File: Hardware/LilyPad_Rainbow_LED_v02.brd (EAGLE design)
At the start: 38.6 x 12.7 mm, 37 parts

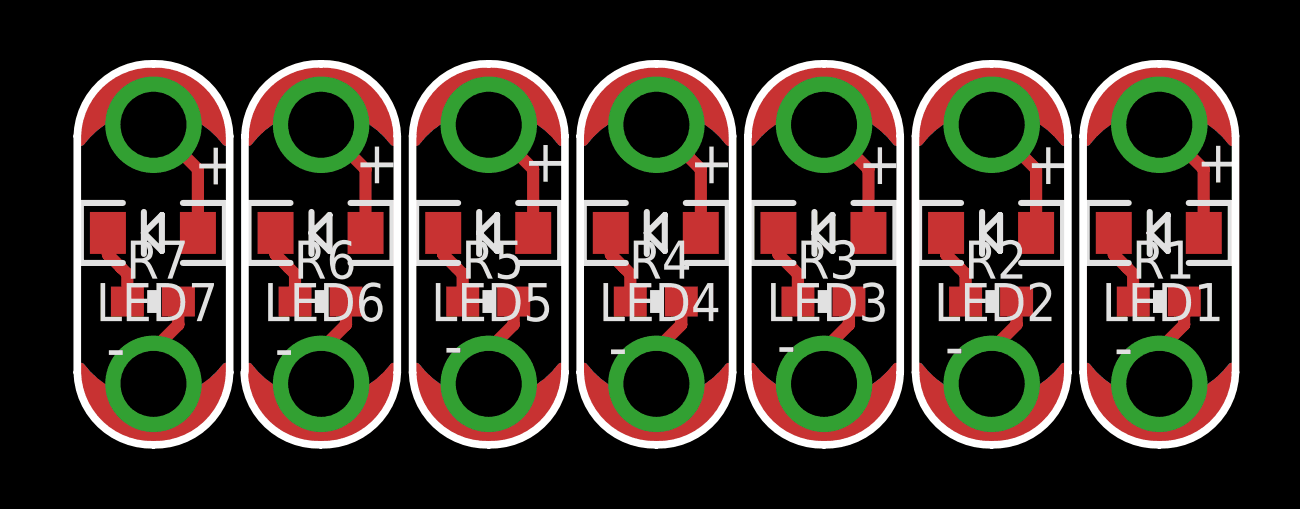
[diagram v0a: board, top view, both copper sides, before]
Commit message: Updated Board File and Sch File per Eng. Design Review
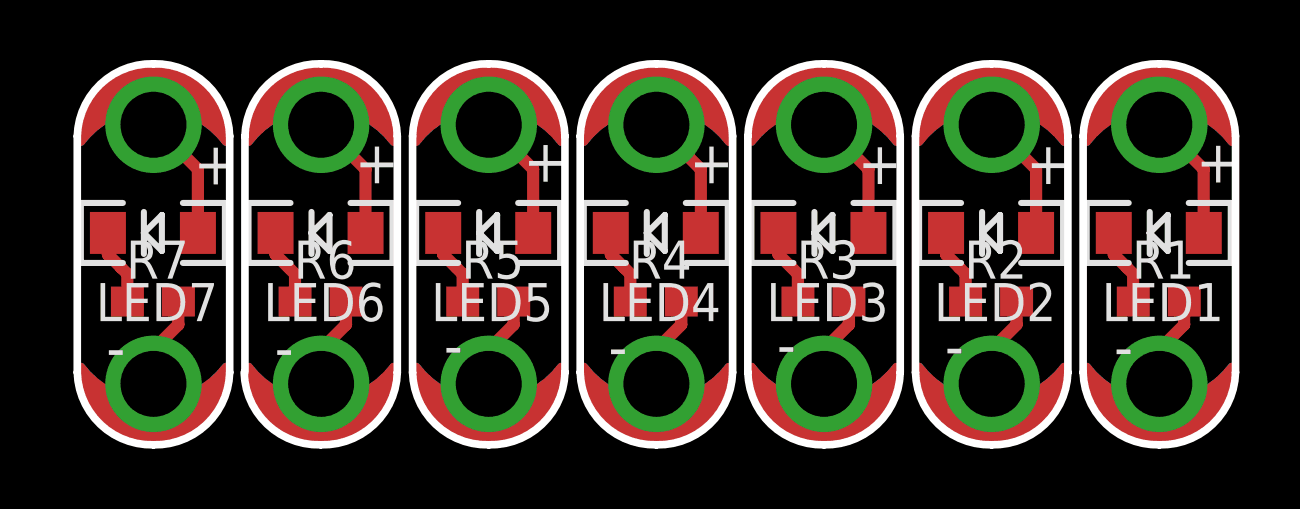
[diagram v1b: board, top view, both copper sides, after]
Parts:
- moved U$1 31.8 mm to (26.7, -11.4)
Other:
- board text added: "0.032" board thickness Purple Solder Mask"
- board text added: "v11"
- board text removed: "0.032" board thickness Purple Silk"
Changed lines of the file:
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@@
 <setting verticaltext="up"/>
 </settings>
-<grid distance="0.001" unitdist="inch" unit="inch" style="lines" multiple="1" display="yes" altdistance="0.005" altunitdist="inch" altunit="inch"/>
+<grid distance="0.05" unitdist="inch" unit="inch" style="lines" multiple="1" display="yes" altdistance="0.005" altunitdist="inch" altunit="inch"/>
 <layers>
 <layer number="1" name="Top" color="4" fill="1" visible="yes" active="yes"/>
@@
 <text x="13.03655" y="1.9558" size="1.4224" layer="22" ratio="15" rot="MR0">-</text>
 <wire x1="25.4" y1="12.065" x2="27.94" y2="9.652" width="0.254" layer="20" curve="-90.018049"/>
-<text x="43.18" y="15.24" size="1.778" layer="47" font="vector" ratio="15">All Units Inches</text>
-<text x="43.18" y="8.89" size="1.778" layer="51" font="vector" ratio="15">0.032" board thickness
-Purple Silk</text>
+<text x="43.18" y="7.62" size="1.778" layer="47" font="vector" ratio="15">All Units Inches</text>
+<text x="41.91" y="1.27" size="1.778" layer="51" font="vector" ratio="15">0.032" board thickness
+Purple Solder Mask</text>
 <text x="45.72" y="-8.89" size="1.778" layer="51" font="vector" ratio="15">L. Buechley </text>
-<text x="15.24" y="-12.7" size="1.778" layer="51" font="vector" ratio="15">M. West</text>
+<text x="45.72" y="-11.43" size="1.778" layer="51" font="vector" ratio="15">M. West</text>
 <dimension x1="3.048" y1="10.033" x2="8.636" y2="10.033" x3="5.842" y3="19.5834" textsize="1.778" textratio="15" layer="49" unit="inch"/>
 <dimension x1="3.048" y1="10.033" x2="3.048" y2="1.397" x3="-1.8796" y3="5.715" textsize="1.778" textratio="15" layer="49" unit="inch"/>
 <dimension x1="3.048" y1="12.065" x2="3.048" y2="-0.635" x3="-5.4356" y3="5.715" textsize="1.778" textratio="15" layer="49" unit="inch"/>
 <wire x1="8.6106" y1="-0.635" x2="6.0706" y2="1.778" width="0.254" layer="20" curve="-90.013536"/>
+<text x="26.67" y="-13.97" size="1.778" layer="51" font="vector" ratio="15">v11</text>
 </plain>
 <attributes>
@@
 <element name="LOGO35" library="LilyPad-Wearables" package="LOGO-L" value="LOGO-LPL" x="36.6268" y="5.4356" rot="MR0"/>
 <element name="FRAME1" library="SparkFun-Aesthetics" package="CREATIVE_COMMONS" value="FRAME-LETTER" x="15.24" y="-8.89"/>
-<element name="U$1" library="SparkFun-Aesthetics" package="REVISION" value="REVISION" x="-5.08" y="-12.7"/>
+<element name="U$1" library="SparkFun-Aesthetics" package="REVISION" value="REVISION" x="26.67" y="-11.43"/>
 </elements>
 <signals>
